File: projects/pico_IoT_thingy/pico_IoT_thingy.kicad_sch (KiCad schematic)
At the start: 58 parts, among them IC1 THVD1406DR, J1 Barrel_Jack_Switch, J2 Conn_01x04, J3 Conn_01x03, J4 Screw_Terminal_01x03, J5 Screw_Terminal_01x04, J6 Conn_02x05_Odd_Even, J7 Conn_01x02, K1 RT314A05, Q1 BC817, SW1 SW_SPST, SW2 SW_SPST, SW3 SW_DIP_x04, U1 TSR_1-2450, U2 SHT31-DIS, U3 TLV1117-33

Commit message: Pico IoT thingy - assign footprints (WIP)
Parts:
- C1, C2, C3, C4, C5, C6, C7, C8: footprint (none) -> Capacitor_SMD:C_1206_3216Metric_Pad1.33x1.80mm_HandSolder
- D1: footprint DIOM5127X229N -> MH_SMAJ24A:DIOM5127X229N
- D3, D5: footprint (none) -> LED_SMD:LED_1206_3216Metric_Pad1.42x1.75mm_HandSolder
- F1: footprint (none) -> MH_MF-SM100:MFSM1002
- IC1: footprint SOIC127P600X175-8N -> Package_SO:SOIC-8_3.9x4.9mm_P1.27mm
- J1: footprint (none) -> MH_Barrel_Jack:TENSILITY_54-00166
- J2: footprint (none) -> Connector_JST:JST_SH_SM04B-SRSS-TB_1x04-1MP_P1.00mm_Horizontal
- J3: footprint (none) -> Connector_PinHeader_2.54mm:PinHeader_1x03_P2.54mm_Horizontal
- J4: footprint (none) -> TerminalBlock:TerminalBlock_MaiXu_MX126-5.0-03P_1x03_P5.00mm
- J5: footprint (none) -> TerminalBlock:TerminalBlock_MaiXu_MX126-5.0-04P_1x04_P5.00mm
- J6: footprint (none) -> Connector_PinHeader_2.54mm:PinHeader_2x05_P2.54mm_Vertical
- J7: footprint (none) -> Connector_PinHeader_2.54mm:PinHeader_1x02_P2.54mm_Vertical
- JP1: footprint (none) -> Jumper:SolderJumper-2_P1.3mm_Open_RoundedPad1.0x1.5mm
- R1, R10, R11, R12, R13, R14, R15, R16, R17, R18, R19, R2, R20, R3, R4, R5, R6, R7, R8, R9: footprint (none) -> Resistor_SMD:R_1206_3216Metric_Pad1.30x1.75mm_HandSolder
- U3: footprint (none) -> Package_TO_SOT_SMD:SOT-223-3_TabPin2
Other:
- note added: "What is QWIIC: https://www.sparkfun.com/qwiic"
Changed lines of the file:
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@@
 		)
 	)
+	(text "What is QWIIC: https://www.sparkfun.com/qwiic"
+		(exclude_from_sim no)
+		(at 304.8 105.41 0)
+		(effects
+			(font
+				(size 1.27 1.27)
+			)
+		)
+	)
 	(text "Transient protection"
 		(exclude_from_sim no)
@@
 			)
 		)
-		(property "Footprint" ""
+		(property "Footprint" "Resistor_SMD:R_1206_3216Metric_Pad1.30x1.75mm_HandSolder"
 			(at 369.57 48.26 0)
 			(effects
@@
 			)
 		)
-		(property "Footprint" ""
+		(property "Footprint" "Connector_PinHeader_2.54mm:PinHeader_1x03_P2.54mm_Horizontal"
 			(at 171.45 88.9 0)
 			(effects
@@
 			)
 		)
-		(property "Footprint" ""
+		(property "Footprint" "Capacitor_SMD:C_1206_3216Metric_Pad1.33x1.80mm_HandSolder"
 			(at 175.26 228.6 0)
 			(effects
@@
 			)
 		)
-		(property "Footprint" ""
+		(property "Footprint" "MH_MF-SM100:MFSM1002"
 			(at 54.61 46.99 0)
 			(effects
@@
 			)
 		)
-		(property "Datasheet" "~"
+		(property "Datasheet" "https://www.mouser.com/catalog/specsheets/bourns_mfsm.pdf"
 			(at 49.53 48.26 0)
 			(effects
@@
 			)
 		)
-		(property "Footprint" ""
+		(property "Footprint" "Resistor_SMD:R_1206_3216Metric_Pad1.30x1.75mm_HandSolder"
 			(at 314.96 69.85 0)
 			(effects
@@
 			)
 		)
-		(property "Footprint" "DIOM5127X229N"
+		(property "Footprint" "MH_SMAJ24A:DIOM5127X229N"
 			(at -35.23 60.96 0)
 			(effects
@@
 			)
 		)
-		(property "Footprint" ""
+		(property "Footprint" "Resistor_SMD:R_1206_3216Metric_Pad1.30x1.75mm_HandSolder"
 			(at 306.07 69.85 0)
 			(effects
@@
 			)
 		)
-		(property "Footprint" ""
+		(property "Footprint" "Capacitor_SMD:C_1206_3216Metric_Pad1.33x1.80mm_HandSolder"
 			(at 73.66 58.42 0)
 			(effects
@@
 			)
 		)
-		(property "Datasheet" "~"
+		(property "Datasheet" "https://www.mouser.com/catalog/specsheets/bourns_mfsm.pdf"
 			(at 73.66 58.42 0)
 			(effects
@@
 			)
 		)
-		(property "Footprint" ""
+		(property "Footprint" "Resistor_SMD:R_1206_3216Metric_Pad1.30x1.75mm_HandSolder"
 			(at 331.47 163.83 0)
 			(effects
@@
 			)
 		)
-		(property "Footprint" ""
+		(property "Footprint" "Capacitor_SMD:C_1206_3216Metric_Pad1.33x1.80mm_HandSolder"
 			(at 33.02 115.57 0)
 			(effects
@@
 			)
 		)
-		(property "Footprint" ""
+		(property "Footprint" "Resistor_SMD:R_1206_3216Metric_Pad1.30x1.75mm_HandSolder"
 			(at 308.61 137.16 0)
 			(effects
@@
 			)
 		)
-		(property "Footprint" ""
+		(property "Footprint" "Resistor_SMD:R_1206_3216Metric_Pad1.30x1.75mm_HandSolder"
 			(at 58.42 254 0)
 			(effects
@@
 			)
 		)
-		(property "Footprint" ""
+		(property "Footprint" "Capacitor_SMD:C_1206_3216Metric_Pad1.33x1.80mm_HandSolder"
 			(at 341.63 48.26 0)
 			(effects
@@
 			)
 		)
-		(property "Footprint" ""
+		(property "Footprint" "Resistor_SMD:R_1206_3216Metric_Pad1.30x1.75mm_HandSolder"
 			(at 241.3 242.57 0)
 			(effects
@@
 			)
 		)
-		(property "Footprint" ""
+		(property "Footprint" "Resistor_SMD:R_1206_3216Metric_Pad1.30x1.75mm_HandSolder"
 			(at 64.77 157.48 0)
 			(effects
@@
 			)
 		)
-		(property "Footprint" ""
+		(property "Footprint" "Connector_PinHeader_2.54mm:PinHeader_2x05_P2.54mm_Vertical"
 			(at 344.17 226.06 0)
 			(effects
@@
 			)
 		)
-		(property "Footprint" ""
+		(property "Footprint" "Capacitor_SMD:C_1206_3216Metric_Pad1.33x1.80mm_HandSolder"
 			(at 63.5 115.57 0)
 			(effects
@@
 			)
 		)
-		(property "Footprint" ""
+		(property "Footprint" "Resistor_SMD:R_1206_3216Metric_Pad1.30x1.75mm_HandSolder"
 			(at 53.34 219.71 0)
 			(effects
@@
 			)
 		)
-		(property "Footprint" ""
+		(property "Footprint" "TerminalBlock:TerminalBlock_MaiXu_MX126-5.0-03P_1x03_P5.00mm"
 			(at 388.62 140.97 0)
 			(effects
@@
 			)
 		)
-		(property "Footprint" ""
+		(property "Footprint" "Connector_JST:JST_SH_SM04B-SRSS-TB_1x04-1MP_P1.00mm_Horizontal"
 			(at 340.36 81.28 0)
 			(effects
@@
 			)
 		)
-		(property "Footprint" ""
+		(property "Footprint" "Capacitor_SMD:C_1206_3216Metric_Pad1.33x1.80mm_HandSolder"
 			(at 328.93 90.17 0)
 			(effects
@@
 			)
 		)
-		(property "Footprint" ""
+		(property "Footprint" "Package_TO_SOT_SMD:SOT-223-3_TabPin2"
 			(at 48.26 105.41 0)
 			(effects
@@
 			)
 		)
-		(property "Footprint" ""
+		(property "Footprint" "TerminalBlock:TerminalBlock_MaiXu_MX126-5.0-04P_1x04_P5.00mm"
 			(at 257.81 210.82 0)
 			(effects
@@
 			)
 		)
-		(property "Footprint" ""
+		(property "Footprint" "Jumper:SolderJumper-2_P1.3mm_Open_RoundedPad1.0x1.5mm"
 			(at 377.19 48.26 0)
 			(effects
@@
 			)
 		)
-		(property "Footprint" ""
+		(property "Footprint" "Resistor_SMD:R_1206_3216Metric_Pad1.30x1.75mm_HandSolder"
 			(at 241.3 247.65 0)
 			(effects
@@
 			)
 		)
-		(property "Footprint" "SOIC127P600X175-8N"
+		(property "Footprint" "Package_SO:SOIC-8_3.9x4.9mm_P1.27mm"
 			(at 209.55 345.11 0)
 			(effects
@@
 			)
 		)
-		(property "Footprint" ""
+		(property "Footprint" "Resistor_SMD:R_1206_3216Metric_Pad1.30x1.75mm_HandSolder"
 			(at 53.34 209.55 0)
 			(effects
@@
 			)
 		)
-		(property "Footprint" ""
+		(property "Footprint" "Connector_PinHeader_2.54mm:PinHeader_1x02_P2.54mm_Vertical"
 			(at 219.71 232.41 0)
 			(effects
@@
 			)
 		)
-		(property "Footprint" ""
+		(property "Footprint" "Resistor_SMD:R_1206_3216Metric_Pad1.30x1.75mm_HandSolder"
 			(at 212.09 87.63 0)
 			(effects
@@
 			)
 		)
-		(property "Footprint" ""
+		(property "Footprint" "Resistor_SMD:R_1206_3216Metric_Pad1.30x1.75mm_HandSolder"
 			(at 377.19 69.85 0)
 			(effects
@@
 			)
 		)
-		(property "Footprint" ""
+		(property "Footprint" "Resistor_SMD:R_1206_3216Metric_Pad1.30x1.75mm_HandSolder"
 			(at 68.58 254 0)
 			(effects
@@
 			)
 		)
-		(property "Footprint" ""
+		(property "Footprint" "Resistor_SMD:R_1206_3216Metric_Pad1.30x1.75mm_HandSolder"
 			(at 207.01 236.22 0)
 			(effects
@@
 			)
 		)
-		(property "Footprint" ""
+		(property "Footprint" "Capacitor_SMD:C_1206_3216Metric_Pad1.33x1.80mm_HandSolder"
 			(at 64.77 167.64 0)
 			(effects
@@
 			)
 		)
-		(property "Footprint" ""
+		(property "Footprint" "Resistor_SMD:R_1206_3216Metric_Pad1.30x1.75mm_HandSolder"
 			(at 78.74 254 0)
 			(effects
@@
 			)
 		)
-		(property "Footprint" ""
+		(property "Footprint" "Resistor_SMD:R_1206_3216Metric_Pad1.30x1.75mm_HandSolder"
 			(at 325.12 160.02 0)
 			(effects
@@
 			)
 		)
-		(property "Footprint" ""
+		(property "Footprint" "Resistor_SMD:R_1206_3216Metric_Pad1.30x1.75mm_HandSolder"
 			(at 53.34 214.63 0)
 			(effects
@@
 			)
 		)
-		(property "Footprint" ""
+		(property "Footprint" "Resistor_SMD:R_1206_3216Metric_Pad1.30x1.75mm_HandSolder"
 			(at 92.71 110.49 0)
 			(effects
@@
 			)
 		)
-		(property "Footprint" ""
+		(property "Footprint" "LED_SMD:LED_1206_3216Metric_Pad1.42x1.75mm_HandSolder"
 			(at 92.71 116.84 0)
 			(effects
@@
 			)
 		)
-		(property "Footprint" ""
+		(property "Footprint" "Resistor_SMD:R_1206_3216Metric_Pad1.30x1.75mm_HandSolder"
 			(at 88.9 254 0)
 			(effects
@@
 			)
 		)
-		(property "Footprint" ""
+		(property "Footprint" "LED_SMD:LED_1206_3216Metric_Pad1.42x1.75mm_HandSolder"
 			(at 308.61 143.51 0)
 			(effects
@@
 			)
 		)
-		(property "Footprint" ""
+		(property "Footprint" "Capacitor_SMD:C_1206_3216Metric_Pad1.33x1.80mm_HandSolder"
 			(at 104.14 58.42 0)
 			(effects
@@
 			)
 		)
-		(property "Footprint" ""
+		(property "Footprint" "MH_Barrel_Jack:TENSILITY_54-00166"
 			(at 34.29 51.816 0)
 			(effects

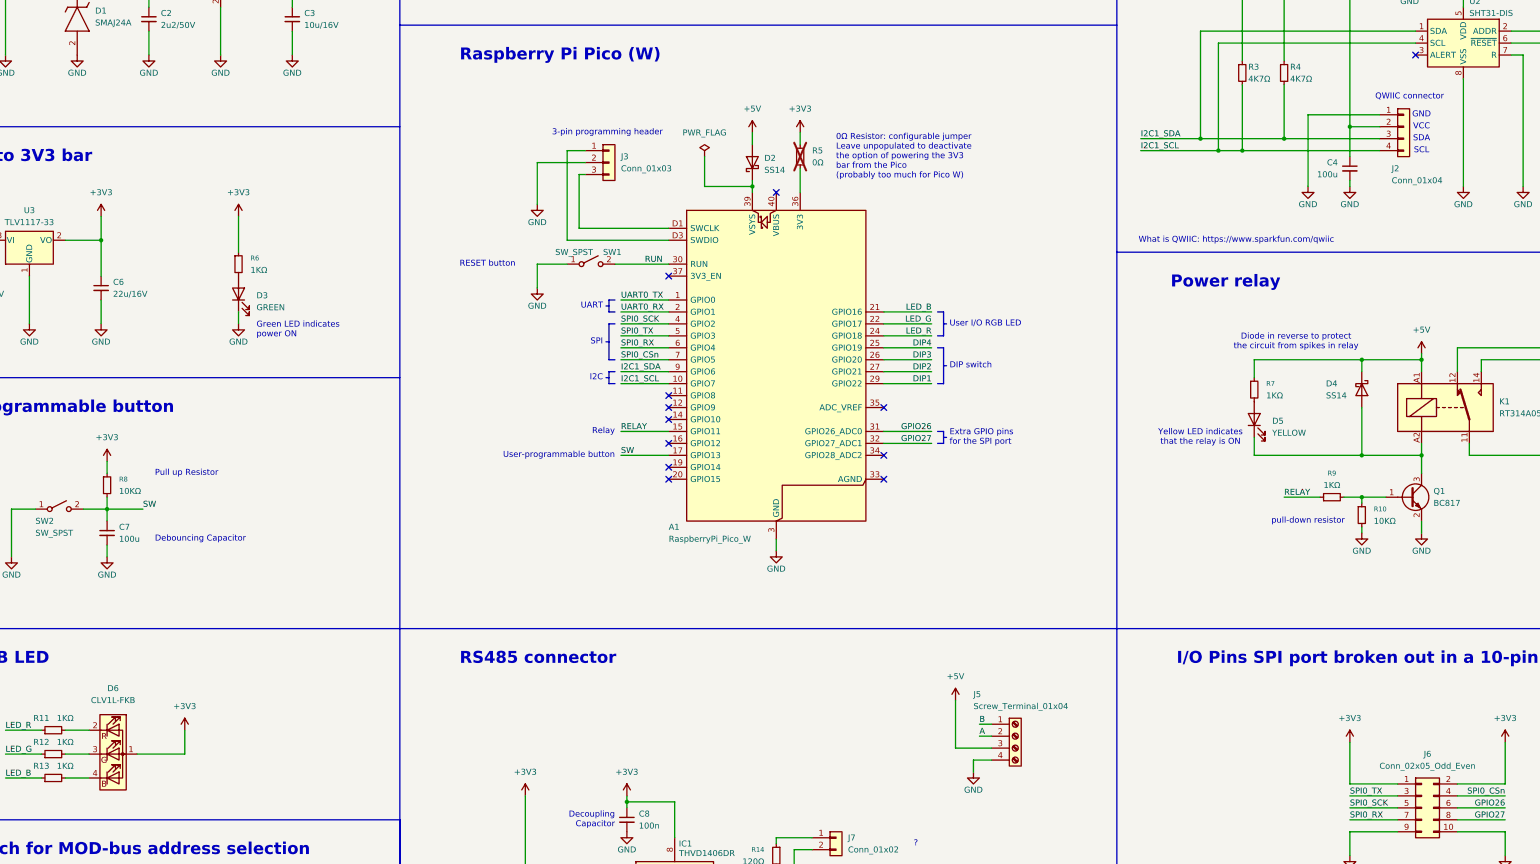
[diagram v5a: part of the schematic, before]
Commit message: Pico IoT thingy - complete footprints assignment
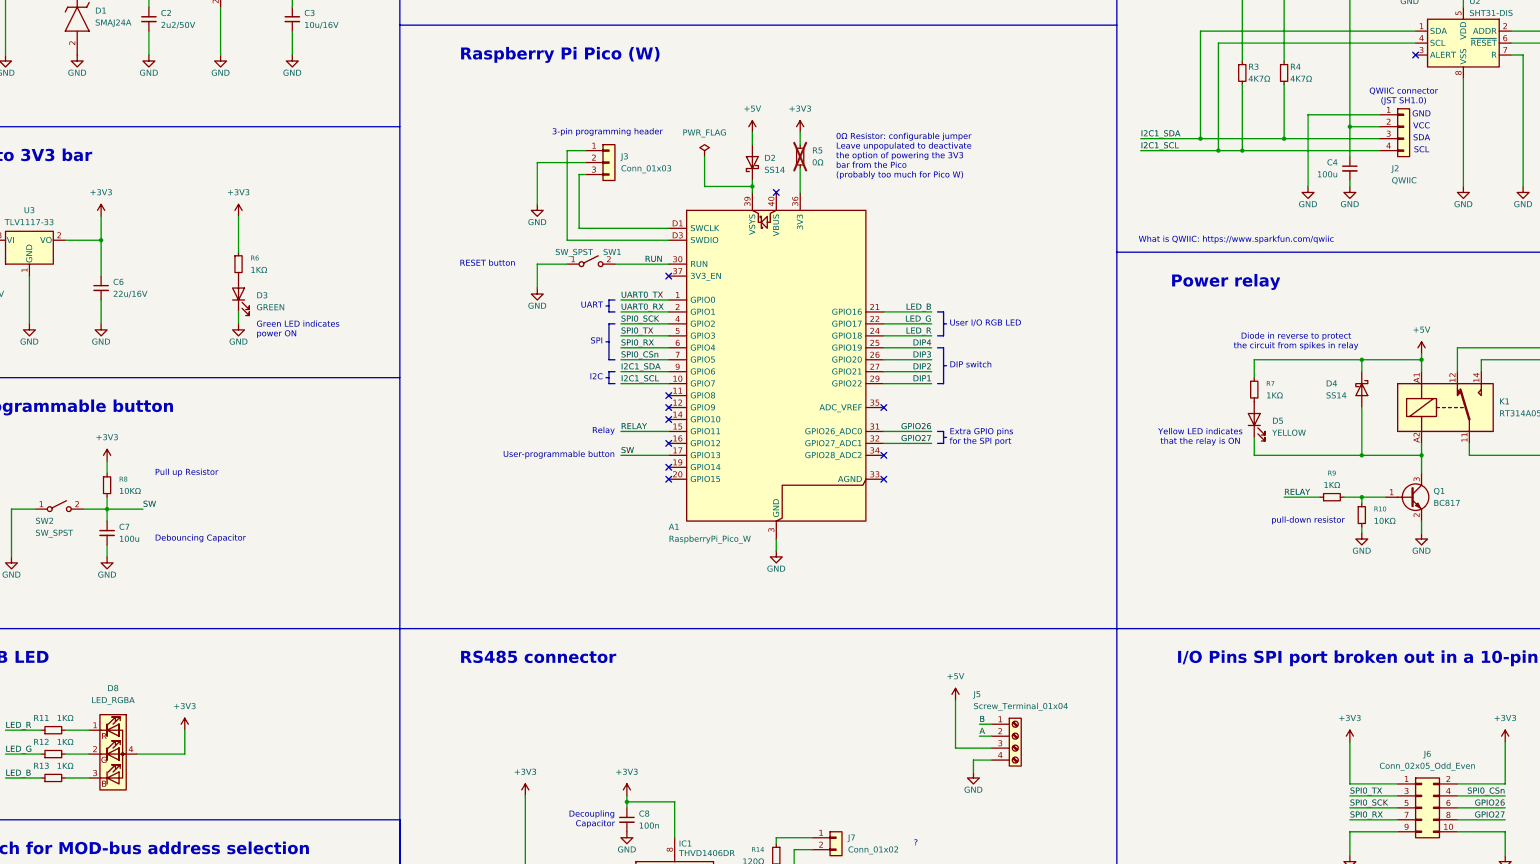
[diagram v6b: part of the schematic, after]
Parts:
- removed D6: CLV1L-FKB, LED_SMD:LED_Cree-PLCC4_3.2x2.8mm_CCW, symbol LED:CLV1L-FKB
- added D8: LED_RGBA, LED_SMD:LED_RGB_1210, symbol Device:LED_RGBA
- H1, H2, H3, H4: footprint (none) -> MountingHole:MountingHole_3.2mm_M3_DIN965_Pad
- J1: footprint MH_Barrel_Jack:TENSILITY_54-00166 -> Connector_BarrelJack:BarrelJack_GCT_DCJ200-10-A_Horizontal
- J2: value Conn_01x04 -> QWIIC
- SW1, SW2: footprint (none) -> Button_Switch_SMD:SW_SPST_Omron_B3FS-101xP
- SW3: footprint (none) -> MH_DIPSWITCH:2194MST
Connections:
- net +3V3: now also D8.4 (A)
- net at R11.2: now also D8.1 (RK)
- net at R12.2: now also D8.2 (GK)
- net at R13.2: now also D8.3 (BK)
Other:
- note added: "QWIIC connector (JST SH1.0)"
- note removed: "QWIIC connector"
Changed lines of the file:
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@@
 		)
 	)
-	(text "QWIIC connector"
+	(text "QWIIC connector\n(JST SH1.0)"
 		(exclude_from_sim no)
-		(at 341.63 74.93 0)
+		(at 340.36 74.93 0)
 		(effects
 			(font
@@
 			)
 		)
-		(property "Footprint" ""
+		(property "Footprint" "MountingHole:MountingHole_3.2mm_M3_DIN965_Pad"
 			(at 215.9 41.91 0)
 			(effects
@@
 			)
 		)
-		(property "Footprint" ""
+		(property "Footprint" "MountingHole:MountingHole_3.2mm_M3_DIN965_Pad"
 			(at 165.1 41.91 0)
 			(effects
@@
 	)
 	(symbol
-		(lib_id "LED:CLV1L-FKB")
-		(at 66.04 214.63 0)
-		(unit 1)
-		(exclude_from_sim no)
-		(in_bom yes)
-		(on_board yes)
-		(dnp no)
-		(fields_autoplaced yes)
-		(property "Reference" "D6"
-			(at 66.04 200.66 0)
-			(effects
-				(font
-					(size 1.27 1.27)
-				)
-			)
-		)
-		(property "Value" "CLV1L-FKB"
-			(at 66.04 203.2 0)
-			(effects
-				(font
-					(size 1.27 1.27)
-				)
-			)
-		)
-		(property "Footprint" "LED_SMD:LED_Cree-PLCC4_3.2x2.8mm_CCW"
-			(at 66.04 215.9 0)
-			(effects
-				(font
-					(size 1.27 1.27)
-				)
-				(hide yes)
-			)
-		)
-		(property "Datasheet" "http://www.cree.com/led-components/media/documents/CLV1L-FKB-1238.pdf"
-			(at 66.04 215.9 0)
-			(effects
-				(font
-					(size 1.27 1.27)
-				)
-				(hide yes)
-			)
-		)
-		(property "Description" "Cree PLCC4 3 in 1 SMD LED"
-			(at 66.04 214.63 0)
-			(effects
-				(font
-					(size 1.27 1.27)
-				)
-				(hide yes)
-			)
-		)
-		(pin "1"
-		)
-		(pin "3"
-		)
-		(pin "2"
-		)
-		(pin "4"
-		)
-		(instances
-			(project ""
-				(path "/976a870b-4bc8-4381-8f7b-7356f08e7273"
-					(reference "D6")
-					(unit 1)
-				)
-			)
-		)
-	)
-	(symbol
 		(lib_id "Device:R_Small")
 		(at 58.42 254 0)
@@
 			)
 		)
-		(property "Footprint" ""
+		(property "Footprint" "MountingHole:MountingHole_3.2mm_M3_DIN965_Pad"
 			(at 190.5 41.91 0)
 			(effects
@@
 			)
 		)
-		(property "Value" "Conn_01x04"
+		(property "Value" "QWIIC"
 			(at 337.82 92.71 0)
 			(effects
@@
 			)
 		)
-		(property "Footprint" ""
+		(property "Footprint" "Button_Switch_SMD:SW_SPST_Omron_B3FS-101xP"
 			(at 54.61 162.56 0)
 			(effects
@@
 			)
 		)
-		(property "Footprint" ""
+		(property "Footprint" "Button_Switch_SMD:SW_SPST_Omron_B3FS-101xP"
 			(at 167.64 110.49 0)
 			(effects
@@
 	)
 	(symbol
+		(lib_id "Device:LED_RGBA")
+		(at 66.04 214.63 0)
+		(unit 1)
+		(exclude_from_sim no)
+		(in_bom yes)
+		(on_board yes)
+		(dnp no)
+		(fields_autoplaced yes)
+		(property "Reference" "D8"
+			(at 66.04 200.66 0)
+			(effects
+				(font
+					(size 1.27 1.27)
+				)
+			)
+		)
+		(property "Value" "LED_RGBA"
+			(at 66.04 203.2 0)
+			(effects
+				(font
+					(size 1.27 1.27)
+				)
+			)
+		)
+		(property "Footprint" "LED_SMD:LED_RGB_1210"
+			(at 66.04 215.9 0)
+			(effects
+				(font
+					(size 1.27 1.27)
+				)
+				(hide yes)
+			)
+		)
+		(property "Datasheet" "~"
+			(at 66.04 215.9 0)
+			(effects
+				(font
+					(size 1.27 1.27)
+				)
+				(hide yes)
+			)
+		)
+		(property "Description" "RGB LED, red/green/blue/anode"
+			(at 66.04 214.63 0)
+			(effects
+				(font
+					(size 1.27 1.27)
+				)
+				(hide yes)
+			)
+		)
+		(pin "4"
+		)
+		(pin "2"
+		)
+		(pin "1"
+		)
+		(pin "3"
+		)
+		(instances
+			(project ""
+				(path "/976a870b-4bc8-4381-8f7b-7356f08e7273"
+					(reference "D8")
+					(unit 1)
+				)
+			)
+		)
+	)
+	(symbol
 		(lib_id "Device:R_Small")
 		(at 207.01 236.22 0)
@@
 			)
 		)
-		(property "Footprint" ""
+		(property "Footprint" "MH_DIPSWITCH:2194MST"
 			(at 45.72 264.16 0)
 			(effects
@@
 			)
 		)
-		(property "Footprint" ""
+		(property "Footprint" "MountingHole:MountingHole_3.2mm_M3_DIN965_Pad"
 			(at 241.3 41.91 0)
 			(effects
@@
 			)
 		)
-		(property "Footprint" "MH_Barrel_Jack:TENSILITY_54-00166"
+		(property "Footprint" "Connector_BarrelJack:BarrelJack_GCT_DCJ200-10-A_Horizontal"
 			(at 34.29 51.816 0)
 			(effects
